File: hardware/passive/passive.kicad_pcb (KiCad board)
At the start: 2 copper layers, 45 x 17 mm, 7 parts, among them J1 I/O, J2 conn_2x2

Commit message: Passive board v3.0
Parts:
- moved J2 30.5 mm to (138.0, 108.5), turned to 0 degrees
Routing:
- net out-: track 21.4 -> 36.6 mm
- net int_coil+: track 22.3 -> 31.3 mm
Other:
- board text added: "XR Spectra Passive v3.0"
- board text removed: "XR Spectra Passive v1.02"

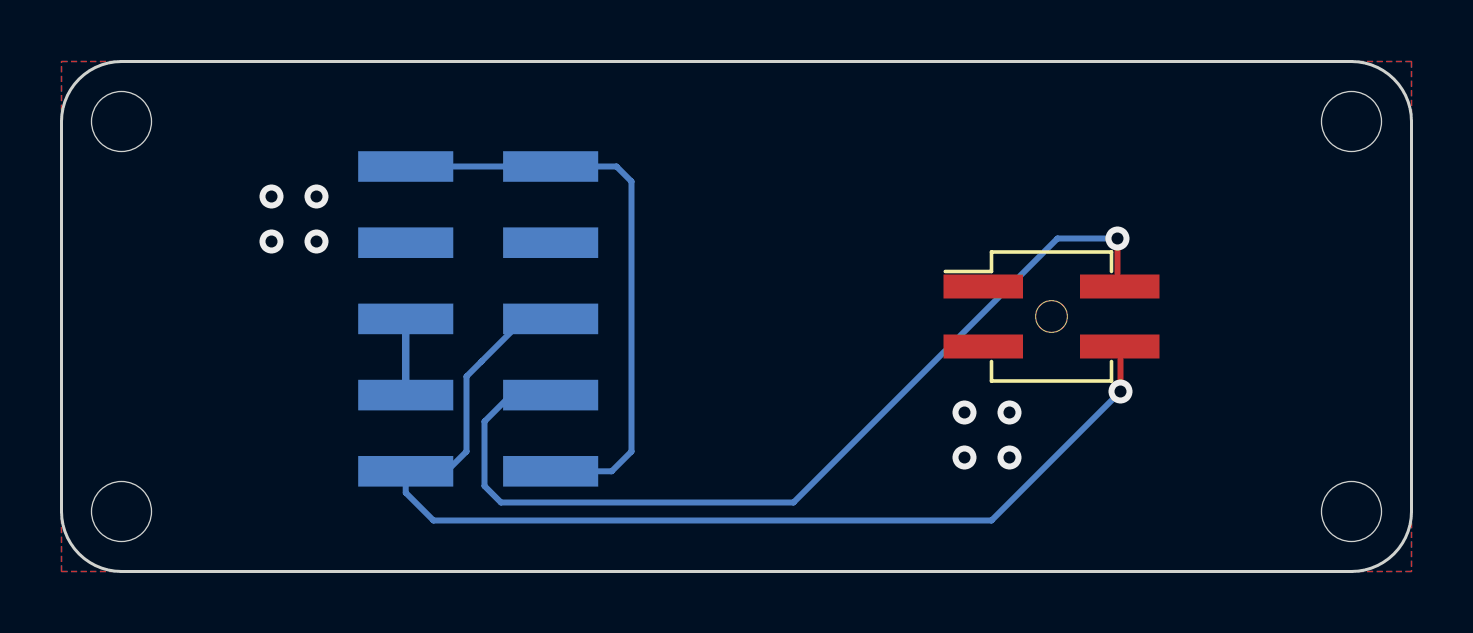
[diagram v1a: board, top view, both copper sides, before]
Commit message: Add labels
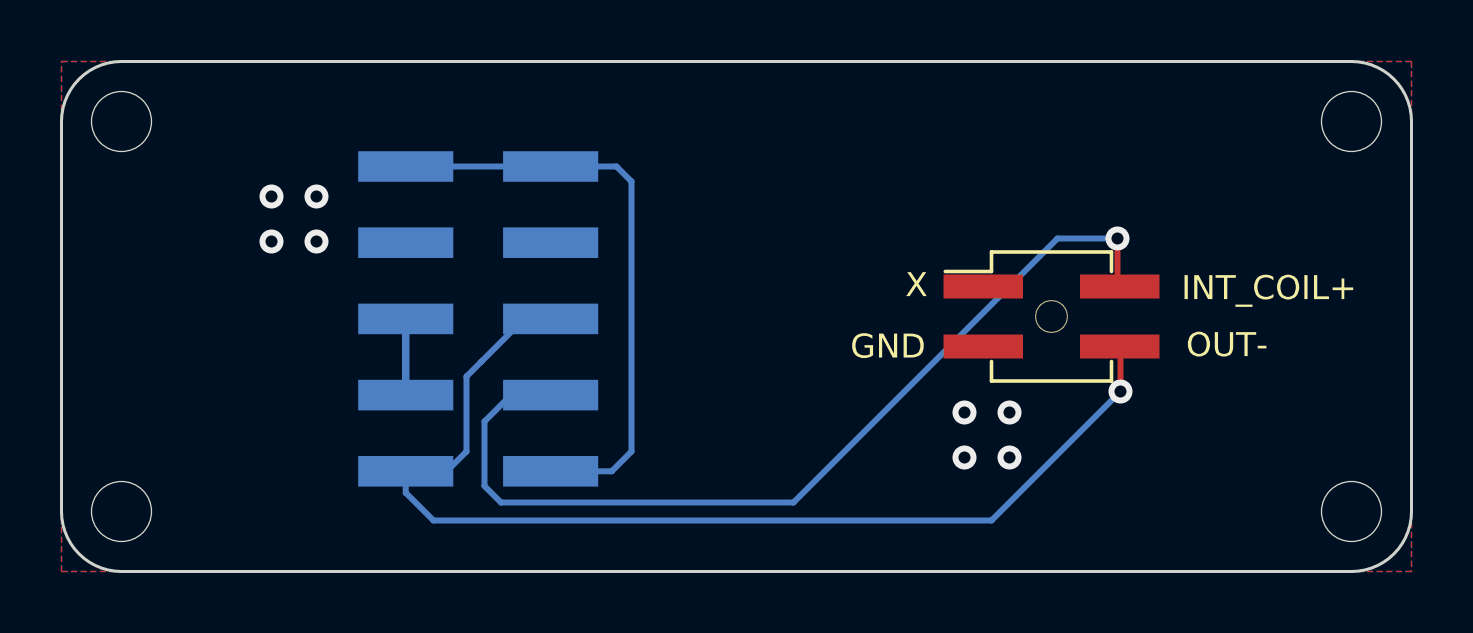
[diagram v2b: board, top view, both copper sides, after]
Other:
- board text added: "GND"
- board text added: "INT_COIL+"
- board text added: "OUT-"
- board text added: "X"
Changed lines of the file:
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@@
     (effects (font (size 0.5 0.5) (thickness 0.125)) (justify mirror))
+  )
+  (gr_text "X" (at 133.5 107.45) (layer "F.SilkS")
+    (effects (font (size 0.8 0.8) (thickness 0.1)))
+  )
+  (gr_text "OUT-" (at 143.85 109.45) (layer "F.SilkS")
+    (effects (font (size 0.8 0.8) (thickness 0.1)))
+  )
+  (gr_text "INT_COIL+" (at 145.25 107.55) (layer "F.SilkS")
+    (effects (font (size 0.8 0.8) (thickness 0.1)))
+  )
+  (gr_text "GND" (at 132.55 109.5) (layer "F.SilkS")
+    (effects (font (size 0.8 0.8) (thickness 0.1)))
   )
   (via (at 136.6 113.2) (size 0.8) (drill 0.4) (layers "F.Cu" "B.Cu") (free) (net 1))
